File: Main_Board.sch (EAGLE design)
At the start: 73 parts, among them U1 RN4020RN4020, U2 LMS8117, U3 5V_BUCK_REG, Y1 MC-30632.768K-E3, Y2 MA-5066-25.0000M-C0

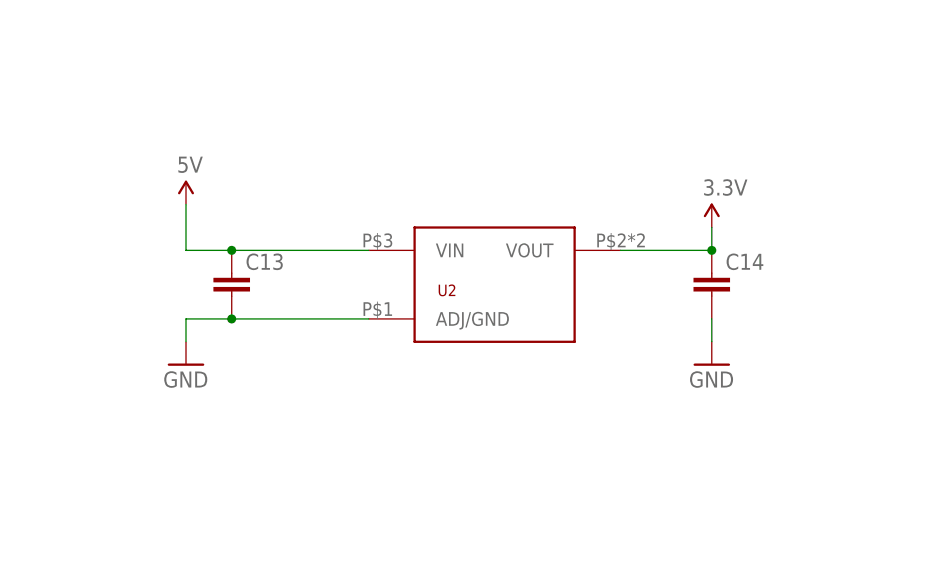
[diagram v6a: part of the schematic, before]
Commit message: Added cap values
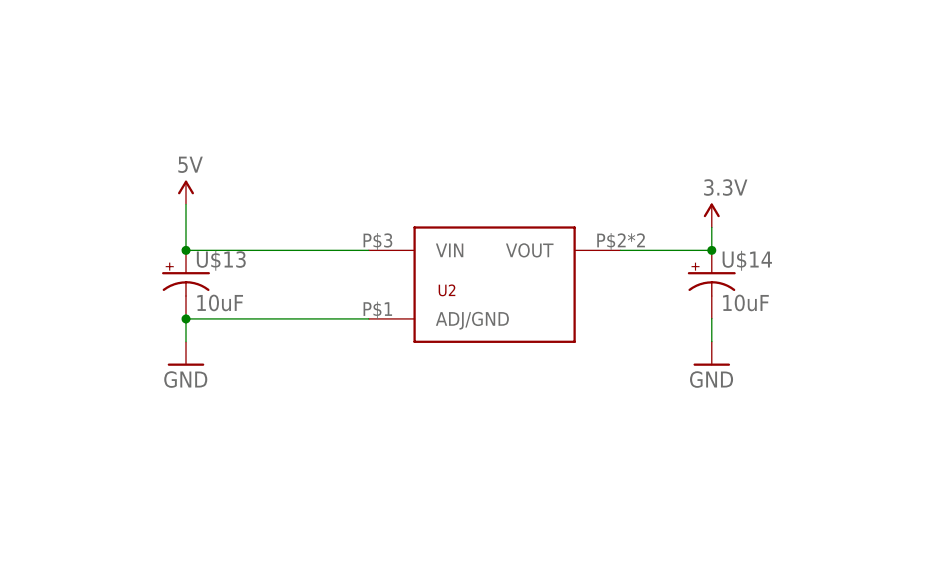
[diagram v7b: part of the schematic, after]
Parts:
- removed C13, C14: (no value), SparkFun-Capacitors:CAP0805
- added U$13, U$14: 10uF, BB8:CAP_POL_PAN
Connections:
- net 3.3V: now also U$14.+; no longer C14.1
- net 5V: now also U$13.+; no longer C13.1
- net GND: now also U$13.-, U$14.-; no longer C13.2, C14.2
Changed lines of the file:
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@@
 <part name="GND17" library="SparkFun-Aesthetics" deviceset="GND" device=""/>
 <part name="SUPPLY13" library="SparkFun-Aesthetics" deviceset="3.3V" device=""/>
-<part name="C13" library="SparkFun-Capacitors" deviceset="CAP" device="0805"/>
-<part name="C14" library="SparkFun-Capacitors" deviceset="CAP" device="0805"/>
 <part name="GND18" library="SparkFun-Aesthetics" deviceset="GND" device=""/>
 <part name="U$9" library="BB8" deviceset="SN74LV4T125" device=""/>
@@
 <part name="GND42" library="SparkFun-Aesthetics" deviceset="GND" device=""/>
 <part name="SUPPLY17" library="SparkFun-Aesthetics" deviceset="5V" device=""/>
+<part name="U$13" library="BB8" deviceset="CAP_POL_PAN" device="" value="10uF"/>
+<part name="U$14" library="BB8" deviceset="CAP_POL_PAN" device="" value="10uF"/>
 </parts>
 <sheets>
@@
 <instance part="GND17" gate="1" x="-129.54" y="-106.68"/>
 <instance part="SUPPLY13" gate="G$1" x="-71.12" y="-91.44"/>
-<instance part="C13" gate="G$1" x="-124.46" y="-99.06"/>
-<instance part="C14" gate="G$1" x="-71.12" y="-99.06"/>
 <instance part="GND18" gate="1" x="-71.12" y="-106.68"/>
 <instance part="U$9" gate="G$1" x="157.48" y="129.54"/>
@@
 <instance part="GND42" gate="1" x="218.44" y="68.58"/>
 <instance part="SUPPLY17" gate="G$1" x="218.44" y="81.28"/>
+<instance part="U$13" gate="G$1" x="-129.54" y="-96.52"/>
+<instance part="U$14" gate="G$1" x="-71.12" y="-96.52"/>
 </instances>
 <busses>
@@
 </segment>
 <segment>
-<pinref part="C13" gate="G$1" pin="2"/>
-<wire x1="-124.46" y1="-101.6" x2="-109.22" y2="-101.6" width="0.1524" layer="91"/>
+<wire x1="-129.54" y1="-101.6" x2="-109.22" y2="-101.6" width="0.1524" layer="91"/>
 <pinref part="GND17" gate="1" pin="GND"/>
 <wire x1="-129.54" y1="-104.14" x2="-129.54" y2="-101.6" width="0.1524" layer="91"/>
-<wire x1="-129.54" y1="-101.6" x2="-124.46" y2="-101.6" width="0.1524" layer="91"/>
-<junction x="-124.46" y="-101.6"/>
 <pinref part="U2" gate="G$1" pin="ADJ/GND"/>
-</segment>
-<segment>
-<pinref part="C14" gate="G$1" pin="2"/>
+<pinref part="U$13" gate="G$1" pin="-"/>
+<junction x="-129.54" y="-101.6"/>
+</segment>
+<segment>
 <pinref part="GND18" gate="1" pin="GND"/>
 <wire x1="-71.12" y1="-101.6" x2="-71.12" y2="-104.14" width="0.1524" layer="91"/>
+<pinref part="U$14" gate="G$1" pin="-"/>
 </segment>
 <segment>
@@
 </segment>
 <segment>
-<pinref part="C13" gate="G$1" pin="1"/>
-<wire x1="-109.22" y1="-93.98" x2="-124.46" y2="-93.98" width="0.1524" layer="91"/>
+<wire x1="-109.22" y1="-93.98" x2="-129.54" y2="-93.98" width="0.1524" layer="91"/>
 <pinref part="SUPPLY12" gate="G$1" pin="5V"/>
-<wire x1="-124.46" y1="-93.98" x2="-129.54" y2="-93.98" width="0.1524" layer="91"/>
 <wire x1="-129.54" y1="-93.98" x2="-129.54" y2="-88.9" width="0.1524" layer="91"/>
-<junction x="-124.46" y="-93.98"/>
 <pinref part="U2" gate="G$1" pin="VIN"/>
+<pinref part="U$13" gate="G$1" pin="+"/>
+<junction x="-129.54" y="-93.98"/>
 </segment>
 <segment>
@@
 </segment>
 <segment>
-<pinref part="C14" gate="G$1" pin="1"/>
 <wire x1="-81.28" y1="-93.98" x2="-71.12" y2="-93.98" width="0.1524" layer="91"/>
 <pinref part="SUPPLY13" gate="G$1" pin="3.3V"/>
 <wire x1="-71.12" y1="-93.98" x2="-71.12" y2="-91.44" width="0.1524" layer="91"/>
+<pinref part="U2" gate="G$1" pin="VOUT"/>
+<pinref part="U$14" gate="G$1" pin="+"/>
 <junction x="-71.12" y="-93.98"/>
-<pinref part="U2" gate="G$1" pin="VOUT"/>
-</segment>
-<segment>
+</segment>
+<segment>

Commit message: Moved parts onto board
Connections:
- removed net N$33: U1.CMD/MLDP
- new net BLU_CMD: U$5.PB1, U1.CMD/MLDP
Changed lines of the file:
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@@
 <pinref part="U1" gate="G$1" pin="UART_RX"/>
 <wire x1="477.52" y1="-180.34" x2="467.36" y2="-180.34" width="0.1524" layer="91"/>
-<label x="467.36" y="-180.34" size="1.778" layer="95"/>
+<label x="464.82" y="-180.34" size="1.778" layer="95"/>
 </segment>
 <segment>
@@
 <segment>
 <pinref part="U1" gate="G$1" pin="UART_TX"/>
-<wire x1="477.52" y1="-175.26" x2="467.36" y2="-175.26" width="0.1524" layer="91"/>
-<label x="467.36" y="-175.26" size="1.778" layer="95"/>
+<wire x1="477.52" y1="-175.26" x2="464.82" y2="-175.26" width="0.1524" layer="91"/>
+<label x="464.82" y="-175.26" size="1.778" layer="95"/>
 </segment>
 </net>
@@
 </segment>
 </net>
-<net name="N$33" class="0">
+<net name="BLU_CMD" class="0">
 <segment>
 <pinref part="U1" gate="G$1" pin="CMD/MLDP"/>
 <wire x1="477.52" y1="-190.5" x2="467.36" y2="-190.5" width="0.1524" layer="91"/>
-<label x="368.3" y="-193.04" size="1.778" layer="95"/>
+<label x="462.28" y="-190.5" size="1.778" layer="95"/>
+</segment>
+<segment>
+<pinref part="U$5" gate="G$1" pin="PB1"/>
+<wire x1="383.54" y1="-17.78" x2="401.32" y2="-17.78" width="0.1524" layer="91"/>
+<label x="393.7" y="-17.78" size="1.778" layer="95"/>
 </segment>
 </net>
